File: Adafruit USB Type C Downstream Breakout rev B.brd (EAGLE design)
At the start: 20.3 x 14 mm, 10 parts

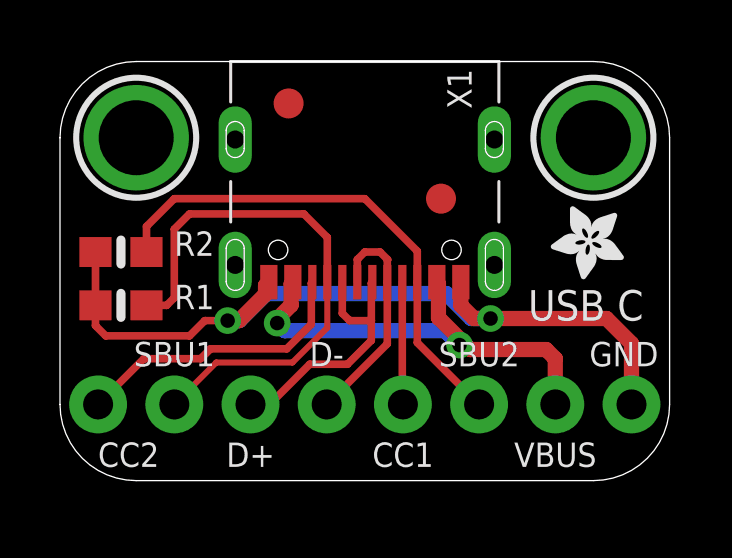
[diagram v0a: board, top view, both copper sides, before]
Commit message: updating to rev b to fix issue #1
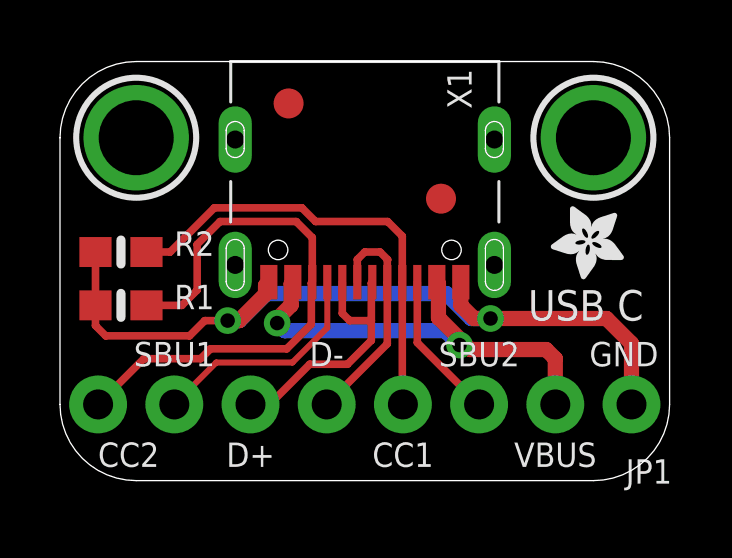
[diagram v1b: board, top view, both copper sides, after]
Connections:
- net CC1: now also R2.2
- net CC2: now also R1.2
- net SBU1: no longer R1.2
- net SBU2: no longer R2.2
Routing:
- net SBU2: track 16.9 -> 4.93 mm
- net CC1: track 4.08 -> 15.1 mm
- net SBU1: track 18.1 -> 7.68 mm
- net CC2: track 9.63 -> 18.9 mm
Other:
- board text added: "downstream (periph.) USB C Breakout"
- board text removed: "downstream USB C Breakout"
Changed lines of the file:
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@@
 <?xml version="1.0" encoding="utf-8"?>
 <!DOCTYPE eagle SYSTEM "eagle.dtd">
-<eagle version="9.3.0">
+<eagle version="9.2.0">
 <drawing>
 <settings>
-<setting alwaysvectorfont="yes"/>
+<setting alwaysvectorfont="no"/>
 <setting keepoldvectorfont="yes"/>
 <setting verticaltext="up"/>
@@
 <layer number="25" name="tNames" color="7" fill="1" visible="no" active="yes"/>
 <layer number="26" name="bNames" color="7" fill="1" visible="no" active="yes"/>
-<layer number="27" name="tValues" color="7" fill="1" visible="no" active="yes"/>
+<layer number="27" name="tValues" color="7" fill="1" visible="yes" active="yes"/>
 <layer number="28" name="bValues" color="7" fill="1" visible="no" active="yes"/>
 <layer number="29" name="tStop" color="7" fill="3" visible="no" active="yes"/>
@@
 <text x="2.286" y="1.27" size="0.8128" layer="21" font="vector" ratio="14" align="top-center">CC2</text>
 <text x="6.604" y="13.462" size="1.016" layer="22" font="vector" ratio="14" rot="MR180">adafruit!</text>
-<text x="10.16" y="4.826" size="1.016" layer="22" font="vector" ratio="14" rot="MR180" align="center">downstream
+<text x="10.16" y="6.858" size="1.016" layer="22" font="vector" ratio="14" distance="100" rot="MR180" align="center">downstream
+(periph.)
 USB C Breakout</text>
 <dimension x1="20.32" y1="-1.27" x2="0" y2="-1.27" x3="10.16" y3="-2.54" textsize="1.778" layer="47" unit="inch"/>
@@
 </plain>
 <attributes>
-<attribute name="REV" value="A"/>
+<attribute name="REV" value="B"/>
 </attributes>
 <variantdefs>
@@
 </autorouter>
 <elements>
-<element name="FID1" library="microbuilder" package="FIDUCIAL_1MM" value="FIDUCIAL_1MM" x="12.7" y="9.398" smashed="yes" rot="R180">
+<element name="FID1" library="microbuilder" package="FIDUCIAL_1MM" value="FIDUCIAL_1MM" x="12.7" y="9.398" rot="R180">
 <attribute name="BOM" value="EXCLUDE" x="-2.54" y="30.988" size="1.778" layer="27" rot="R180" display="off"/>
 </element>
-<element name="FID2" library="microbuilder" package="FIDUCIAL_1MM" value="FIDUCIAL_1MM" x="7.62" y="12.573" smashed="yes" rot="R180">
+<element name="FID2" library="microbuilder" package="FIDUCIAL_1MM" value="FIDUCIAL_1MM" x="7.62" y="12.573" rot="R180">
 <attribute name="BOM" value="EXCLUDE" x="-11.43" y="34.163" size="1.778" layer="27" rot="R180" display="off"/>
 </element>
-<element name="U$1" library="microbuilder" package="MOUNTINGHOLE_2.5_PLATED" value="MOUNTINGHOLE2.5" x="17.78" y="11.43" smashed="yes" rot="R180">
+<element name="U$1" library="microbuilder" package="MOUNTINGHOLE_2.5_PLATED" value="MOUNTINGHOLE2.5" x="17.78" y="11.43" rot="R180">
 <attribute name="BOM" value="EXCLUDE" x="-7.62" y="13.97" size="1.778" layer="27" rot="R180" display="off"/>
 </element>
-<element name="U$2" library="microbuilder" package="MOUNTINGHOLE_2.5_PLATED" value="MOUNTINGHOLE2.5" x="2.54" y="11.43" smashed="yes" rot="R180">
+<element name="U$2" library="microbuilder" package="MOUNTINGHOLE_2.5_PLATED" value="MOUNTINGHOLE2.5" x="2.54" y="11.43" rot="R180">
 <attribute name="BOM" value="EXCLUDE" x="-12.7" y="24.13" size="1.778" layer="27" rot="R180" display="off"/>
 </element>
-<element name="X1" library="microbuilder" package="USB_C_CUSB31-CFM2AX-01-X" value="" x="10.16" y="13.97" smashed="yes" rot="R180">
+<element name="X1" library="microbuilder" package="USB_C_CUSB31-CFM2AX-01-X" value="" x="10.16" y="13.97" rot="R180">
 <attribute name="NAME" x="12.91" y="13.72" size="0.8128" layer="25" font="vector" ratio="18" rot="R270"/>
 <attribute name="VALUE" x="11.66" y="13.72" size="0.4064" layer="27" ratio="10" rot="R270"/>
 </element>
-<element name="U$3" library="microbuilder" package="ADAFRUIT_2.5MM" value="" x="18.796" y="9.144" smashed="yes" rot="R180"/>
-<element name="JP1" library="microbuilder" package="1X08_ROUND_76" value="" x="10.16" y="2.54" smashed="yes" rot="R180">
+<element name="U$3" library="microbuilder" package="ADAFRUIT_2.5MM" value="" x="18.796" y="9.144" rot="R180"/>
+<element name="JP1" library="microbuilder" package="1X08_ROUND_76" value="" x="10.16" y="2.54" rot="R180">
 <attribute name="VALUE" x="20.32" y="5.715" size="0.4064" layer="27" ratio="10" rot="R180"/>
 </element>
-<element name="R1" library="microbuilder" package="0603-NO" value="5.1K" x="2.032" y="5.842" smashed="yes">
+<element name="R1" library="microbuilder" package="0603-NO" value="5.1K" x="2.032" y="5.842">
 <attribute name="NAME" x="3.81" y="5.715" size="0.8128" layer="25" font="vector" ratio="18"/>
 <attribute name="VALUE" x="3.81" y="5.08" size="0.4064" layer="27" font="vector" ratio="10"/>
 </element>
-<element name="R2" library="microbuilder" package="0603-NO" value="5.1K" x="2.032" y="7.62" smashed="yes">
+<element name="R2" library="microbuilder" package="0603-NO" value="5.1K" x="2.032" y="7.62">
 <attribute name="NAME" x="3.81" y="7.493" size="0.8128" layer="25" font="vector" ratio="18"/>
 <attribute name="VALUE" x="3.81" y="6.858" size="0.4064" layer="27" font="vector" ratio="10"/>
 </element>
-<element name="U$8" library="microbuilder" package="PCBFEAT-REV-040" value="" x="1.6256" y="4.8768" smashed="yes" rot="MR180">
+<element name="U$8" library="microbuilder" package="PCBFEAT-REV-040" value="" x="1.6256" y="4.8768" rot="MR180">
 <attribute name="REV" x="1.27" y="5.3848" size="1.016" layer="22" ratio="20" rot="MR180"/>
 </element>
@@
 <wire x1="11.41" y1="6.615" x2="11.41" y2="2.56" width="0.254" layer="1"/>
 <wire x1="11.41" y1="2.56" x2="11.43" y2="2.54" width="0.254" layer="1"/>
+<contactref element="R2" pad="2"/>
+<wire x1="5.14461875" y1="9.0932" x2="8.06338125" y2="9.0932" width="0.254" layer="1"/>
+<wire x1="2.882" y1="7.62" x2="3.67141875" y2="7.62" width="0.254" layer="1"/>
+<wire x1="8.06338125" y1="9.0932" x2="8.52058125" y2="8.636" width="0.254" layer="1"/>
+<wire x1="3.67141875" y1="7.62" x2="5.14461875" y2="9.0932" width="0.254" layer="1"/>
+<wire x1="10.922" y1="8.636" x2="8.52058125" y2="8.636" width="0.254" layer="1"/>
+<wire x1="11.41" y1="6.615" x2="11.41" y2="8.148" width="0.254" layer="1"/>
+<wire x1="11.41" y1="8.148" x2="10.922" y2="8.636" width="0.254" layer="1"/>
 </signal>
 <signal name="CC2">
@@
 <wire x1="2.794" y1="4.064" x2="1.27" y2="2.54" width="0.254" layer="1"/>
 <wire x1="4.68741875" y1="4.064" x2="2.794" y2="4.064" width="0.254" layer="1"/>
+<contactref element="R1" pad="2"/>
+<wire x1="8.41" y1="6.615" x2="8.41" y2="8.1" width="0.254" layer="1"/>
+<wire x1="8.41" y1="8.1" x2="7.874" y2="8.636" width="0.254" layer="1"/>
+<wire x1="4.572" y1="7.874" x2="4.572" y2="6.35" width="0.254" layer="1"/>
+<wire x1="4.572" y1="6.35" x2="4.064" y2="5.842" width="0.254" layer="1"/>
+<wire x1="4.064" y1="5.842" x2="2.882" y2="5.842" width="0.254" layer="1"/>
+<wire x1="7.874" y1="8.636" x2="5.334" y2="8.636" width="0.254" layer="1"/>
+<wire x1="5.334" y1="8.636" x2="4.572" y2="7.874" width="0.254" layer="1"/>
 </signal>
 <signal name="SBU1">
 <contactref element="X1" pad="A8"/>
 <contactref element="JP1" pad="7"/>
-<contactref element="R1" pad="2"/>
 <wire x1="8.91" y1="6.615" x2="8.91" y2="5.1" width="0.2032" layer="1"/>
 <wire x1="8.91" y1="5.1" x2="7.747" y2="3.937" width="0.2032" layer="1"/>
 <wire x1="7.747" y1="3.937" x2="5.207" y2="3.937" width="0.2032" layer="1"/>
 <wire x1="5.207" y1="3.937" x2="3.81" y2="2.54" width="0.2032" layer="1"/>
-<wire x1="8.91" y1="6.615" x2="8.91" y2="8.108" width="0.254" layer="1"/>
-<wire x1="8.91" y1="8.108" x2="8.128" y2="8.89" width="0.254" layer="1"/>
-<wire x1="4.318" y1="8.89" x2="3.81" y2="8.382" width="0.254" layer="1"/>
-<wire x1="3.81" y1="8.382" x2="3.81" y2="6.096" width="0.254" layer="1"/>
-<wire x1="3.81" y1="6.096" x2="3.556" y2="5.842" width="0.254" layer="1"/>
-<wire x1="3.556" y1="5.842" x2="2.882" y2="5.842" width="0.254" layer="1"/>
-<wire x1="8.128" y1="8.89" x2="4.318" y2="8.89" width="0.254" layer="1"/>
 </signal>
 <signal name="SBU2">
 <contactref element="X1" pad="B8"/>
 <contactref element="JP1" pad="3"/>
-<contactref element="R2" pad="2"/>
 <wire x1="11.91" y1="6.615" x2="11.91" y2="4.6" width="0.254" layer="1"/>
 <wire x1="11.91" y1="4.6" x2="13.97" y2="2.54" width="0.254" layer="1"/>
-<wire x1="2.882" y1="7.62" x2="2.882" y2="8.47" width="0.254" layer="1"/>
-<wire x1="2.882" y1="8.47" x2="3.81" y2="9.398" width="0.254" layer="1"/>
-<wire x1="10.16" y1="9.398" x2="3.81" y2="9.398" width="0.254" layer="1"/>
-<wire x1="11.91" y1="6.615" x2="11.91" y2="7.648" width="0.254" layer="1"/>
-<wire x1="11.91" y1="7.648" x2="10.16" y2="9.398" width="0.254" layer="1"/>
 </signal>
 </signals>
